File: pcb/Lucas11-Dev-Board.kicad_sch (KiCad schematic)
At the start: 2 parts, among them J1 Conn_01x04, U1 XIAO-RP2350-SMD

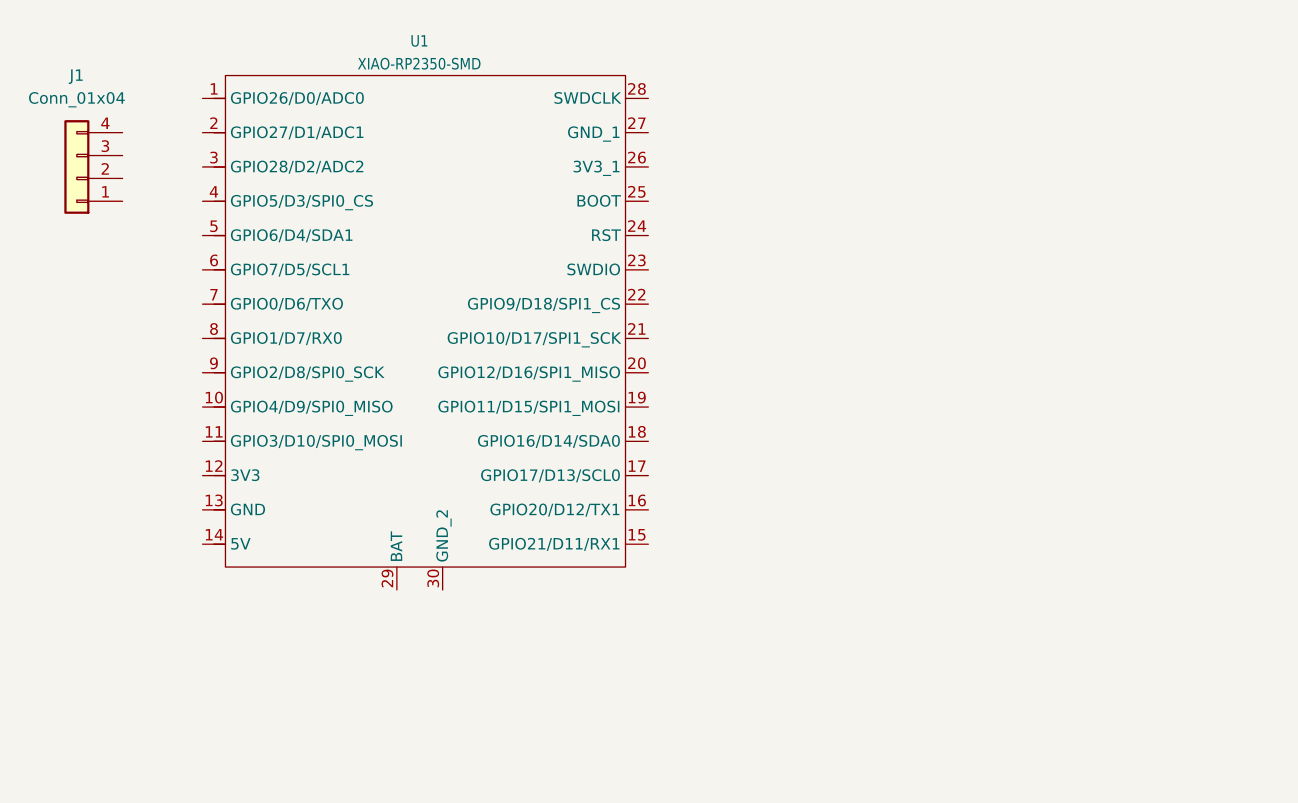
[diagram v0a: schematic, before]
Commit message: Added Leds and keys and finished the pcb part.
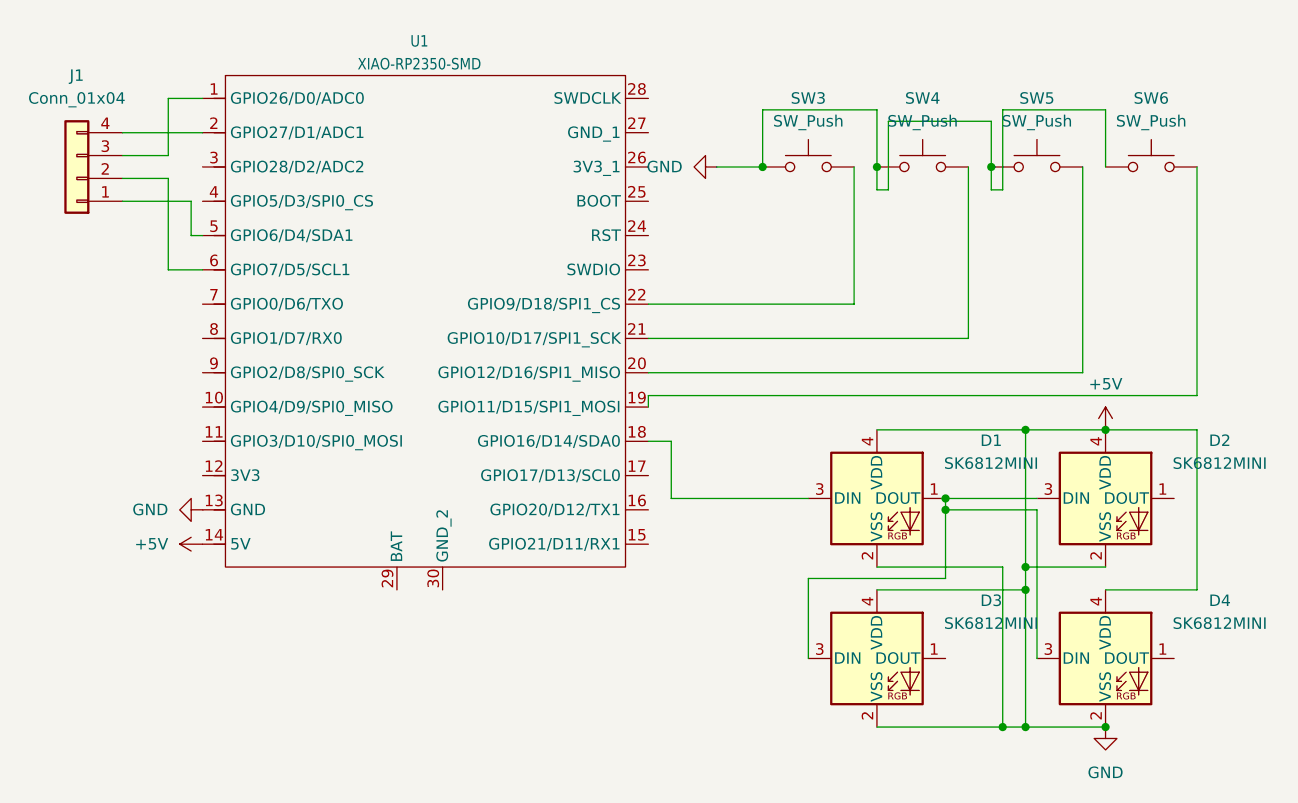
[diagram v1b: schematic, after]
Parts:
- added D1, D2, D3, D4: SK6812MINI, LED_SMD:LED_SK6812MINI_PLCC4_3.5x3.5mm_P1.75mm, symbol LED:SK6812MINI
- added SW3, SW4, SW5, SW6: SW_Push, symbol Switch:SW_Push
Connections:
- net at U1.1 (GPIO26/D0/ADC0): now also J1.3 (Pin_3)
- net +5V: now reaches U1.13 (GND)
- net +5V: now also U1.14 (5V), D1.2 (VSS), D1.4 (VDD), D2.2 (VSS), D2.4 (VDD), D3.2 (VSS), D3.4 (VDD), D4.2 (VSS), D4.4 (VDD), SW3.1, SW4.1, SW5.1, SW6.1
- net at U1.18 (GPIO16/D14/SDA0): now also D1.3 (DIN)
- net at U1.19 (GPIO11/D15/SPI1_MOSI): now also SW6.2
- net at U1.2 (GPIO27/D1/ADC1): now also J1.4 (Pin_4)
- net at U1.20 (GPIO12/D16/SPI1_MISO): now also SW5.2
- net at U1.21 (GPIO10/D17/SPI1_SCK): now also SW4.2
- net at U1.22 (GPIO9/D18/SPI1_CS): now also SW3.2
- net at U1.5 (GPIO6/D4/SDA1): now also J1.1 (Pin_1)
- net at U1.6 (GPIO7/D5/SCL1): now also J1.2 (Pin_2)
- new net: D1.1 (DOUT), D2.3 (DIN), D3.3 (DIN), D4.3 (DIN)

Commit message: Logo wasent centered XD
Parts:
- J1: footprint (none) -> OLED_Screen:SSD1306-0.91-OLED-4pin-128x32
- SW3, SW4, SW5, SW6: footprint (none) -> Button_Switch_Keyboard:SW_Cherry_MX_1.00u_PCB
- U1: footprint (none) -> OPL:XIAO-RP2350-SMD
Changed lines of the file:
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@@
 			)
 		)
-		(property "Footprint" ""
+		(property "Footprint" "Button_Switch_Keyboard:SW_Cherry_MX_1.00u_PCB"
 			(at 144.78 33.02 0)
 			(effects
@@
 			)
 		)
-		(property "Footprint" ""
+		(property "Footprint" "Button_Switch_Keyboard:SW_Cherry_MX_1.00u_PCB"
 			(at 132.08 33.02 0)
 			(effects
@@
 			)
 		)
-		(property "Footprint" ""
+		(property "Footprint" "OPL:XIAO-RP2350-SMD"
 			(at 88.9 41.91 0)
 			(effects
@@
 			)
 		)
-		(property "Footprint" ""
+		(property "Footprint" "OLED_Screen:SSD1306-0.91-OLED-4pin-128x32"
 			(at 50.8 39.37 0)
 			(effects
@@
 			)
 		)
-		(property "Footprint" ""
+		(property "Footprint" "Button_Switch_Keyboard:SW_Cherry_MX_1.00u_PCB"
 			(at 157.48 33.02 0)
 			(effects
@@
 			)
 		)
-		(property "Footprint" ""
+		(property "Footprint" "Button_Switch_Keyboard:SW_Cherry_MX_1.00u_PCB"
 			(at 170.18 33.02 0)
 			(effects

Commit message: a
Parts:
- removed U1: XIAO-RP2350-SMD, OPL:XIAO-RP2350-SMD, symbol OPL:XIAO-RP2350-SMD
- added U2: XIAO-RP2350-DIP, OPL:XIAO-RP2350-DIP, symbol OPL:XIAO-RP2350-DIP
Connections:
- net +5V: now also U2.14 (VBUS); no longer D1.2 (VSS), D2.2 (VSS), D3.2 (VSS), D4.2 (VSS), SW3.1, SW4.1, SW5.1, SW6.1
- net at SW4.2: now also U2.10 (GPIO4/D9/SPI_MISO)
- net at D3.1 (DOUT): now also D4.3 (DIN)
- net at D1.1 (DOUT), D2.3 (DIN): no longer D3.3 (DIN), D4.3 (DIN)
- net at D1.3 (DIN): now also U2.7 (GPIO0/D6/TX0)
- net at SW3.2: now also U2.11 (GPIO3/D10/SPI0_MOSI)
- net at J1.3 (Pin_3): now also U2.1 (GPIO26/D0/ADC0)
- net at SW6.2: now also U2.8 (GPIO1/D7/RX0)
- net at J1.4 (Pin_4): now also U2.2 (GPIO27/D1/ADC1)
- net at SW5.2: now also U2.9 (GPIO2/D8/SPI0_SCK)
- net at J1.1 (Pin_1): now also U2.5 (GPIO6/D4/SDA1)
- net at J1.2 (Pin_2): now also U2.6 (GPIO7/D5/SCL1)
- net at D2.1 (DOUT): now also D3.3 (DIN)
- new net GND: D1.2 (VSS), D2.2 (VSS), D3.2 (VSS), D4.2 (VSS), SW3.1, SW4.1, SW5.1, SW6.1, U2.13 (GND)
